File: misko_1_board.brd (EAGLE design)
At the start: 115 x 115 mm, 147 parts, among them IC1 ATMEGA1281-16AU, IC10 ORG1510-MK4, IC11 TPS3808G33DBVT, IC12 LTC4425, IC13 RN4678_BT_MODULE, IC14 ADXL345, IC15 74HCT1G32, IC16 FM25W256-SOIC, IC17 MICROSD_SPI_MODE, IC18 FH12-30S-0.5SH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

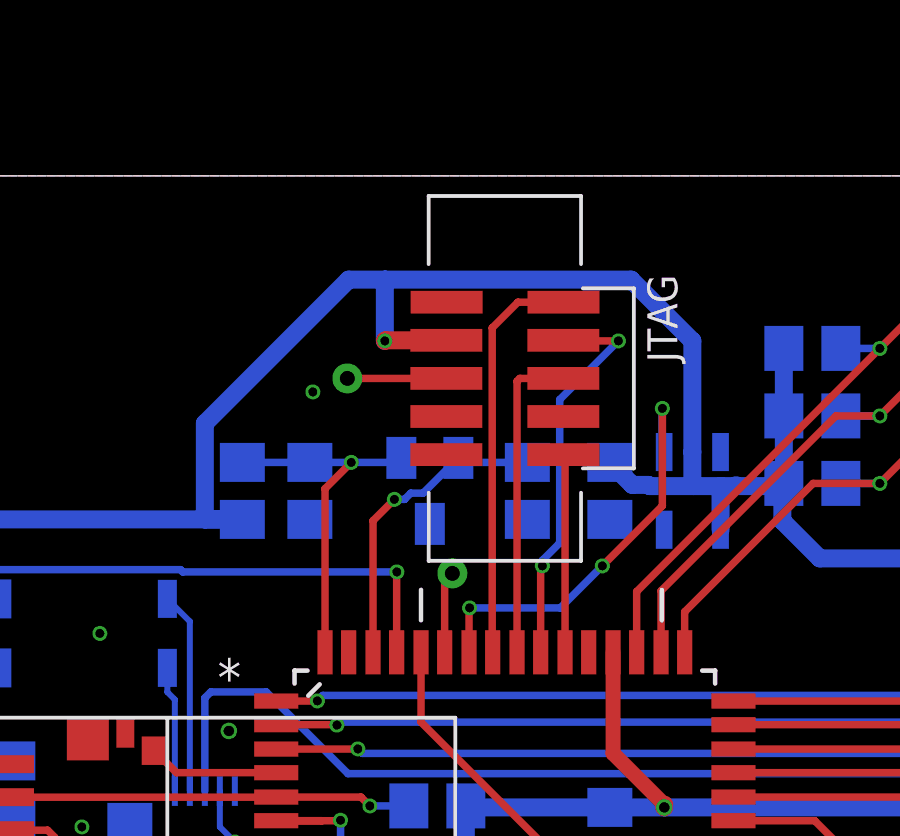
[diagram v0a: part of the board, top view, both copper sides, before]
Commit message: - corrected JTAG 1.27mm 10pin header.lbr; pinout was pairwise swapped - corrected board layout to accommodate new JTAG header orientation
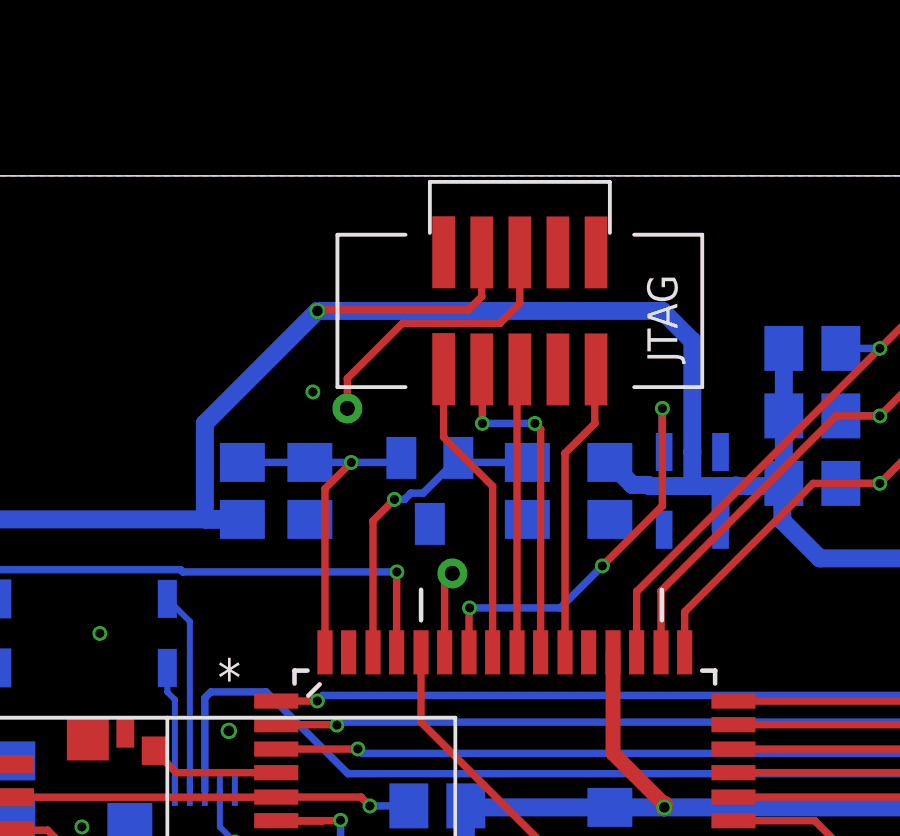
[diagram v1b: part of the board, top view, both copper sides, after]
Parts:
- moved CONN1 2.30 mm to (48.0, 68.5), turned to 0 degrees
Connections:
- net GND: now also CONN1.10_GND, CONN1.2_GND; no longer CONN1.GND1, CONN1.GND2
- net JTAG_TCL_PIN: now also CONN1.1_JTAG_TCK; no longer CONN1.TCL
- net JTAG_TDI_PIN: now also CONN1.9_JTAG_TDI; no longer CONN1.TDI
- net JTAG_TDO_PIN: now also CONN1.3_JTAG_TDO; no longer CONN1.TDO
- net JTAG_TMS_PIN: now also CONN1.5_JTAG_TMS; no longer CONN1.TMS
- net RESET: now also CONN1.6_JTAG_RST; no longer CONN1.RESET
- net VCC: now also CONN1.4_VCC; no longer CONN1.VCC
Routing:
- net RESET: track 58.6 -> 64.8 mm
- net JTAG_TCL_PIN: track 13.6 -> 10.1 mm
- net JTAG_TDI_PIN: track 6.61 -> 9.86 mm
- net VCC: track 505.9 -> 508.1 mm
- net JTAG_TDO_PIN: track 13.3 -> 11.3 mm
- net JTAG_TMS_PIN: track 10.6 -> 9.47 mm

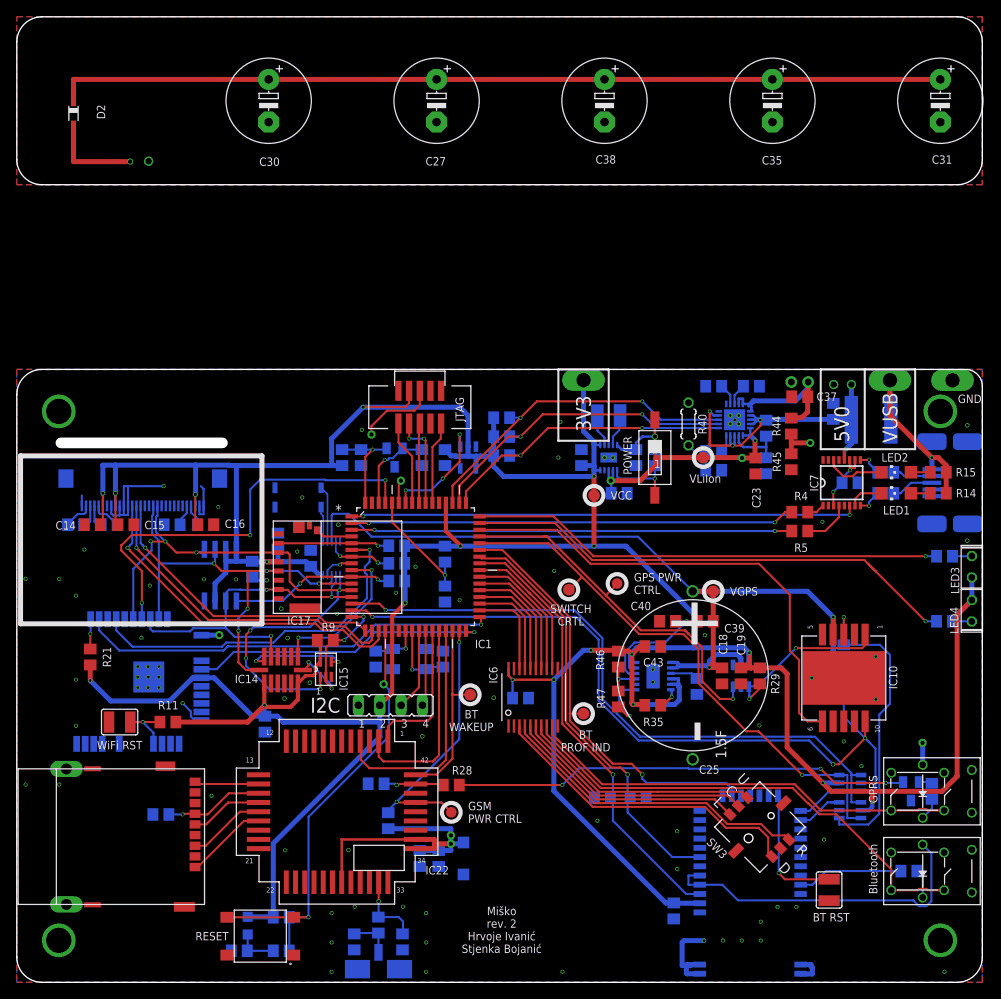
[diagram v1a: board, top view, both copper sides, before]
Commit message: - added zener protection diodes to wifi, bluetooth modules and 5v0 input
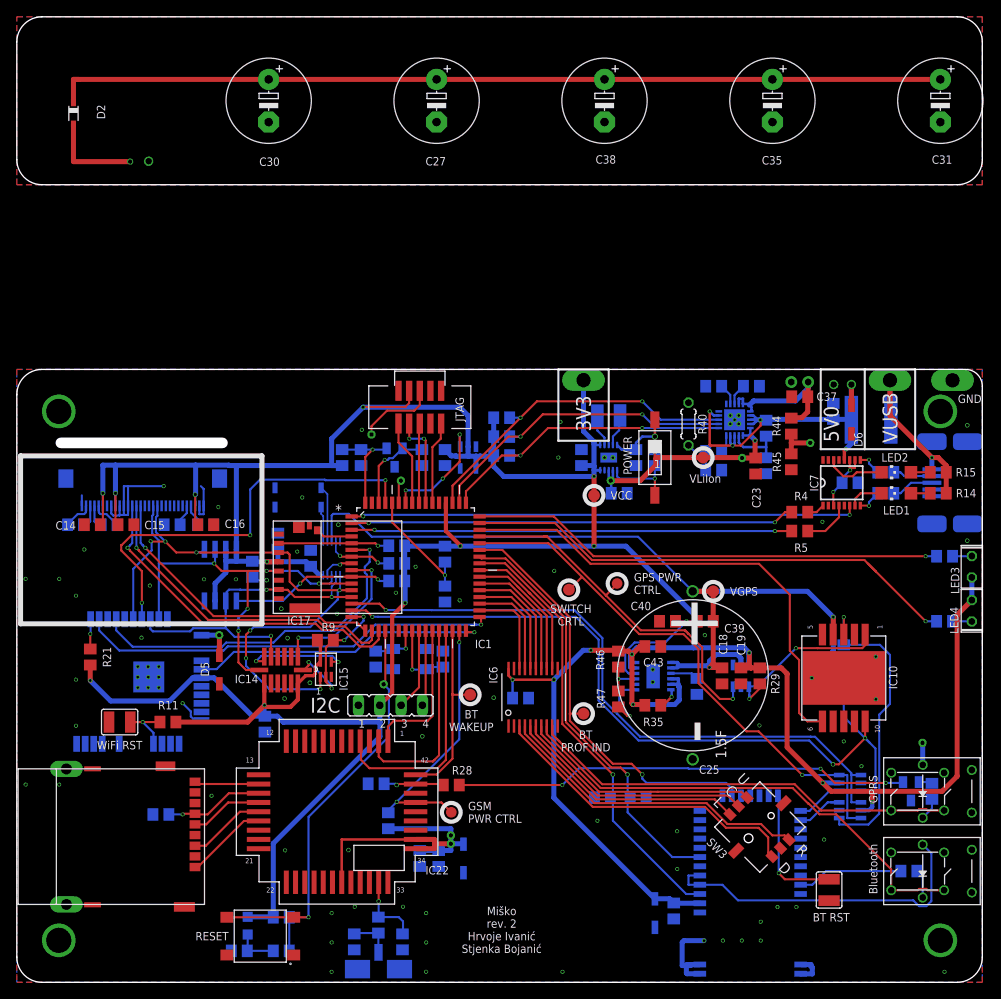
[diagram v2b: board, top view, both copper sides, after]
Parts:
- added D4: BZT52C3V3-E3-08, zener:SOD123
- added D5: BZT52C4V3-E3-18, zener:SOD123
- added D6: 1N4733AW-TP, zener:SOD123
- D3: value MMSZ5231B-DIO -> BZT52C5V1-E3-18; device diode:SOD123 -> zener:SOD123
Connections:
- net 5V0: now also D6.C
- net GND: now also D4.A, D5.A, D6.A
- net VCC: now also D4.C
- net V_LIION+: now also D5.C
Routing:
- net 5V0: track 50.4 -> 52.9 mm
- net V_LIION+: track 57.0 -> 59.3 mm
- net VCC: track 508.1 -> 508.6 mm
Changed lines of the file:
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@@
 <layer number="20" name="Dimension" color="15" fill="1" visible="yes" active="yes"/>
 <layer number="21" name="tPlace" color="7" fill="1" visible="yes" active="yes"/>
-<layer number="22" name="bPlace" color="7" fill="1" visible="yes" active="yes"/>
+<layer number="22" name="bPlace" color="7" fill="1" visible="no" active="yes"/>
 <layer number="23" name="tOrigins" color="15" fill="1" visible="yes" active="yes"/>
-<layer number="24" name="bOrigins" color="15" fill="1" visible="yes" active="yes"/>
+<layer number="24" name="bOrigins" color="15" fill="1" visible="no" active="yes"/>
 <layer number="25" name="tNames" color="7" fill="1" visible="yes" active="yes"/>
-<layer number="26" name="bNames" color="7" fill="1" visible="yes" active="yes"/>
+<layer number="26" name="bNames" color="7" fill="1" visible="no" active="yes"/>
 <layer number="27" name="tValues" color="7" fill="1" visible="no" active="yes"/>
 <layer number="28" name="bValues" color="7" fill="1" visible="no" active="yes"/>
@@
 <layer number="38" name="bTest" color="7" fill="1" visible="no" active="yes"/>
 <layer number="39" name="tKeepout" color="4" fill="11" visible="yes" active="yes"/>
-<layer number="40" name="bKeepout" color="1" fill="11" visible="yes" active="yes"/>
+<layer number="40" name="bKeepout" color="1" fill="11" visible="no" active="yes"/>
 <layer number="41" name="tRestrict" color="4" fill="10" visible="yes" active="yes"/>
-<layer number="42" name="bRestrict" color="1" fill="10" visible="yes" active="yes"/>
+<layer number="42" name="bRestrict" color="1" fill="10" visible="no" active="yes"/>
 <layer number="43" name="vRestrict" color="2" fill="10" visible="no" active="yes"/>
 <layer number="44" name="Drills" color="7" fill="1" visible="yes" active="yes"/>
 <layer number="45" name="Holes" color="7" fill="1" visible="yes" active="yes"/>
 <layer number="46" name="Milling" color="3" fill="1" visible="yes" active="yes"/>
-<layer number="47" name="Measures" color="7" fill="1" visible="no" active="yes"/>
+<layer number="47" name="Measures" color="7" fill="1" visible="yes" active="yes"/>
 <layer number="48" name="Document" color="7" fill="1" visible="yes" active="yes"/>
 <layer number="49" name="Reference" color="7" fill="1" visible="no" active="yes"/>
 <layer number="50" name="dxf" color="7" fill="1" visible="no" active="no"/>
 <layer number="51" name="tDocu" color="7" fill="1" visible="yes" active="yes"/>
-<layer number="52" name="bDocu" color="7" fill="1" visible="yes" active="yes"/>
+<layer number="52" name="bDocu" color="7" fill="1" visible="no" active="yes"/>
 <layer number="53" name="tGND_GNDA" color="7" fill="9" visible="no" active="no"/>
 <layer number="54" name="bGND_GNDA" color="1" fill="9" visible="no" active="no"/>
@@
 <text x="102" y="13.5" size="1" layer="21" font="vector" rot="R90" align="center">Bluetooth</text>
 <text x="102" y="23" size="1" layer="21" font="vector" rot="R90" align="center">GPRS</text>
-<text x="98.25" y="66.5" size="1.778" layer="21" font="vector" rot="R90" align="center">5V0</text>
+<text x="97" y="66.5" size="1.778" layer="21" font="vector" rot="R90" align="center">5V0</text>
 <text x="93.5" y="61" size="1.778" layer="22" font="vector" rot="MR270" align="center">LiPo</text>
 </plain>
@@
 </element>
 <element name="C29" library="rcl" package="C0805" value="10µF" x="78.25" y="8.5" smashed="yes" rot="MR270">
-<attribute name="NAME" x="76.005" y="8.585" size="1" layer="26" font="vector" rot="MR90" align="center"/>
+<attribute name="NAME" x="78.255" y="4.835" size="1" layer="26" font="vector" rot="MR90" align="center"/>
 <attribute name="VALUE" x="80.79" y="9.77" size="1.27" layer="28" rot="MR270"/>
 </element>
@@
 <attribute name="VALUE" x="47.71" y="13.48" size="1.27" layer="28" rot="MR90"/>
 </element>
-<element name="D3" library="diode" library_urn="urn:adsk.eagle:library:210" package="SOD123" value="MMSZ5231B-DIO" x="53.2" y="14.75" smashed="yes" rot="MR270">
+<element name="D3" library="zener" library_urn="urn:adsk.eagle:library:449000" package="SOD123" package3d_urn="urn:adsk.eagle:package:449003/1" value="BZT52C5V1-E3-18" x="53.2" y="14.75" smashed="yes" rot="MR270">
 <attribute name="NAME" x="55.17" y="14.745" size="1" layer="26" font="vector" rot="MR90" align="center"/>
 <attribute name="VALUE" x="55.5" y="15.85" size="1.27" layer="28" rot="MR270"/>
@@
 <attribute name="VALUE" x="70.48" y="60.79" size="1.27" layer="28" rot="MR180"/>
 </element>
+<element name="D5" library="zener" library_urn="urn:adsk.eagle:library:449000" package="SOD123" package3d_urn="urn:adsk.eagle:package:449003/1" value="BZT52C4V3-E3-18" x="24.13" y="37.25" smashed="yes" rot="R270">
+<attribute name="NAME" x="22.4" y="37.29" size="1" layer="25" font="vector" rot="R270" align="center"/>
+<attribute name="VALUE" x="21.59" y="39.79" size="1.016" layer="27" ratio="18" rot="R270"/>
+</element>
+<element name="D4" library="zener" library_urn="urn:adsk.eagle:library:449000" package="SOD123" package3d_urn="urn:adsk.eagle:package:449003/1" value="BZT52C3V3-E3-08" x="76" y="8.25" smashed="yes" rot="MR270">
+<attribute name="NAME" x="73.98" y="8.29" size="1.016" layer="26" font="vector" rot="MR270" align="center"/>
+<attribute name="VALUE" x="78.54" y="10.79" size="1.016" layer="28" ratio="18" rot="MR270"/>
+</element>
+<element name="D6" library="zener" library_urn="urn:adsk.eagle:library:449000" package="SOD123" package3d_urn="urn:adsk.eagle:package:449003/1" value="1N4733AW-TP" x="99.415" y="67.03" smashed="yes" rot="R270">
+<attribute name="NAME" x="100.235" y="64.65" size="1" layer="25" font="vector" rot="R270" align="center"/>
+<attribute name="VALUE" x="96.875" y="69.57" size="1.016" layer="27" ratio="18" rot="R270"/>
+</element>
 </elements>
 <signals>
@@
 <wire x1="26.155" y1="51.5734" x2="26.155" y2="61.514221875" width="0.6" layer="16"/>
 <wire x1="26.155" y1="61.514221875" x2="26.119221875" y2="61.55" width="0.6" layer="16"/>
-<wire x1="63.965665625" y1="36.04305625" x2="63.965665625" y2="22.789325" width="0.6" layer="16"/>
 <wire x1="58.57" y1="36.531925" x2="58.57" y2="37.375" width="0.3" layer="1"/>
 <wire x1="59.05886875" y1="36.04305625" x2="63.965665625" y2="36.04305625" width="0.3" layer="1"/>
@@
 <wire x1="56.75" y1="62.7" x2="56.75" y2="61.5" width="0.6" layer="16"/>
 <wire x1="56.75" y1="61.5" x2="58" y2="60.25" width="0.6" layer="16"/>
-<wire x1="77.304990625" y1="9.45" x2="78.25" y2="9.45" width="0.6" layer="16"/>
-<wire x1="63.965665625" y1="22.789325" x2="77.304990625" y2="9.45" width="0.6" layer="16"/>
-<wire x1="78.25" y1="9.45" x2="78.28" y2="9.42" width="0.6" layer="16"/>
+<wire x1="78.28" y1="9.42" x2="78.25" y2="9.45" width="0.6" layer="16"/>
 <wire x1="78.28" y1="9.42" x2="81.355" y2="9.42" width="0.6" layer="16"/>
 <via x="59.05886875" y="36.04305625" extent="1-16" drill="0.3"/>
@@
 <wire x1="41.25" y1="68.5" x2="52.75" y2="68.5" width="0.6" layer="16"/>
 <wire x1="52.75" y1="68.5" x2="53.75" y2="67.5" width="0.6" layer="16"/>
+<contactref element="D4" pad="C"/>
+<wire x1="76" y1="9.95" x2="77.75" y2="9.95" width="0.6" layer="16"/>
+<wire x1="77.75" y1="9.95" x2="78.28" y2="9.42" width="0.6" layer="16"/>
+<wire x1="63.965665625" y1="21.984334375" x2="76" y2="9.95" width="0.6" layer="16"/>
+<wire x1="63.965665625" y1="36.04305625" x2="63.965665625" y2="21.984334375" width="0.6" layer="16"/>
 </signal>
 <signal name="GND">
@@
 <contactref element="IC6" pad="!EN!"/>
 <contactref element="C45" pad="2"/>
+<contactref element="D5" pad="A"/>
+<contactref element="D4" pad="A"/>
+<contactref element="D6" pad="A"/>
 <wire x1="85.5" y1="67" x2="85.49" y2="67.01" width="0" layer="19" extent="16-16"/>
 <wire x1="32.25" y1="41" x2="31.5" y2="44.5" width="0" layer="19" extent="1-1"/>
@@
 <wire x1="89.25" y1="66.95" x2="89.25" y2="67.029665625" width="0.6" layer="16"/>
 <wire x1="89.25" y1="67.029665625" x2="89.229665625" y2="67.05" width="0.6" layer="16"/>
+<contactref element="D6" pad="C"/>
+<wire x1="99.415" y1="68.73" x2="99.415" y2="71.185" width="0.6" layer="1"/>
+<wire x1="99.415" y1="71.185" x2="99.4" y2="71.2" width="0.6" layer="1"/>
 <wire x1="13.5" y1="97.75" x2="82.5282" y2="68" width="0" layer="19" extent="16-16"/>
 </signal>
@@
 <wire x1="51.7" y1="15.7" x2="51.7" y2="16.5" width="0.6" layer="16"/>
 <wire x1="51.7" y1="16.5" x2="53.2" y2="16.5" width="0.6" layer="16"/>
-<wire x1="53.2" y1="16.5" x2="53.2" y2="16.65" width="0.6" layer="16"/>
+<wire x1="53.2" y1="16.5" x2="53.2" y2="16.45" width="0.6" layer="16"/>
 <wire x1="49.75" y1="17.02" x2="49.75" y2="16.5" width="0.6" layer="1"/>
 <wire x1="49.75" y1="16.5" x2="49.75" y2="15.92" width="0.6" layer="1"/>
@@
 <wire x1="93.5" y1="67.25" x2="92.3" y2="67.25" width="0.6" layer="1"/>
 <wire x1="92.3" y1="67.25" x2="92.25" y2="67.2" width="0.6" layer="1"/>
+<contactref element="D5" pad="C"/>
+<wire x1="24.13" y1="38.95" x2="24.13" y2="41.33" width="0.6" layer="1"/>
+<wire x1="24.13" y1="41.33" x2="24.11" y2="41.35" width="0.6" layer="1"/>
 <wire x1="51.7" y1="18.3" x2="85.998" y2="68.8896" width="0" layer="19" extent="16-16"/>
-<wire x1="24.11" y1="41.35" x2="38.7" y2="17.02" width="0" layer="19" extent="1-1"/>
+<wire x1="24.13" y1="38.95" x2="38.7" y2="17.02" width="0" layer="19" extent="1-1"/>
 </signal>
 <signal name="VGPS" class="1">
@@
 with this version.
 </note>
+<note version="8.3" severity="warning">
+Since Version 8.3, EAGLE supports URNs for individual library
+assets (packages, symbols, and devices). The URNs of those assets
+will not be understood (or retained) with this version.
+</note>
+<note version="8.3" severity="warning">
+Since Version 8.3, EAGLE supports the association of 3D packages
+with devices in libraries, schematics, and board files. Those 3D
+packages will not be understood (or retained) with this version.
+</note>
 </compatibility>
